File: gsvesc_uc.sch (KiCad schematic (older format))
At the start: 13 parts

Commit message: SCM Fertig
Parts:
- removed C? (x5): 10u0, symbol Device:C
- added C10, C11, C12, C13, C8: 10u0/16V, Capacitor_SMD:C_0805_2012Metric, symbol Device:C
- C3, C4, C5: renamed from C?; footprint (none) -> Capacitor_SMD:C_0805_2012Metric
- C6, C7, C9: renamed from C?; value 10u0 -> 10u0/16V; footprint (none) -> Capacitor_SMD:C_0805_2012Metric
- Y1: renamed from Y?; value Crystal_GND24 -> ABM3B 8MHz; footprint (none) -> Crystal:Crystal_SMD_5032-4Pin_5.0x3.2mm
- gave numbers to parts that had none: 1
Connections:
- net GND: now also C10.1, C11.1, C12.1, C13.1, C8.1
- net VCC: now also C10.2, C11.2, C12.2, C13.2, C8.2
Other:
- moved on the sheet: C6
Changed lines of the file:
@@
 $EndDescr
 $Comp
-L MCU_ST_STM32F4:STM32F405RGTx U?
+L MCU_ST_STM32F4:STM32F405RGTx U1
 U 1 1 5BFF9EEA
 P 4150 4200
-F 0 "U?" H 3600 2450 50  0000 C CNN
+F 0 "U1" H 3600 2450 50  0000 C CNN
 F 1 "STM32F405RGTx" H 3600 2350 50  0000 C CNN
 F 2 "Package_QFP:LQFP-64_10x10mm_P0.5mm" H 3550 2500 50  0001 R CNN
@@
 	3450 5800 3200 5800
 $Comp
-L Device:Crystal_GND24 Y?
+L Device:Crystal_GND24 Y1
 U 1 1 5C00BFEF
 P 1900 3800
-F 0 "Y?" H 1700 4100 50  0000 L CNN
-F 1 "Crystal_GND24" H 1250 4000 50  0000 L CNN
-F 2 "" H 1900 3800 50  0001 C CNN
+F 0 "Y1" H 1700 4100 50  0000 L CNN
+F 1 "ABM3B 8MHz" H 1250 4000 50  0000 L CNN
+F 2 "Crystal:Crystal_SMD_5032-4Pin_5.0x3.2mm" H 1900 3800 50  0001 C CNN
 F 3 "~" H 1900 3800 50  0001 C CNN
 	1    1900 3800
@@
 	2400 3900 3450 3900
 $Comp
-L Device:C C?
+L Device:C C3
 U 1 1 5C0116B6
 P 2250 3600
-F 0 "C?" V 2100 3700 50  0000 C CNN
+F 0 "C3" V 2100 3700 50  0000 C CNN
 F 1 "15p0" V 2200 3750 50  0000 C CNN
-F 2 "" H 2288 3450 50  0001 C CNN
+F 2 "Capacitor_SMD:C_0805_2012Metric" H 2288 3450 50  0001 C CNN
 F 3 "~" H 2250 3600 50  0001 C CNN
 	1    2250 3600
@@
 $EndComp
 $Comp
-L Device:C C?
+L Device:C C4
 U 1 1 5C01170C
 P 2250 4000
-F 0 "C?" V 2200 3850 50  0000 C CNN
+F 0 "C4" V 2200 3850 50  0000 C CNN
 F 1 "15p0" V 2300 3850 50  0000 C CNN
-F 2 "" H 2288 3850 50  0001 C CNN
+F 2 "Capacitor_SMD:C_0805_2012Metric" H 2288 3850 50  0001 C CNN
 F 3 "~" H 2250 4000 50  0001 C CNN
 	1    2250 4000
@@
 	2400 3800 2050 3800
 $Comp
-L Device:C C?
+L Device:C C6
 U 1 1 5C01B300
-P 2750 3300
-F 0 "C?" H 2635 3254 50  0000 R CNN
-F 1 "10u0" H 2635 3345 50  0000 R CNN
-F 2 "" H 2788 3150 50  0001 C CNN
-F 3 "~" H 2750 3300 50  0001 C CNN
-	1    2750 3300
+P 2700 3300
+F 0 "C6" H 2650 3200 50  0000 R CNN
+F 1 "10u0/16V" H 2700 3400 50  0000 R CNN
+F 2 "Capacitor_SMD:C_0805_2012Metric" H 2738 3150 50  0001 C CNN
+F 3 "~" H 2700 3300 50  0001 C CNN
+	1    2700 3300
 	-1   0    0    1
 $EndComp
 $Comp
-L Device:C C?
+L Device:C C7
 U 1 1 5C01B37C
 P 3150 3300
-F 0 "C?" H 3035 3254 50  0000 R CNN
-F 1 "10u0" H 3035 3345 50  0000 R CNN
-F 2 "" H 3188 3150 50  0001 C CNN
+F 0 "C7" H 3150 3200 50  0000 R CNN
+F 1 "10u0/16V" H 3150 3400 50  0000 R CNN
+F 2 "Capacitor_SMD:C_0805_2012Metric" H 3188 3150 50  0001 C CNN
 F 3 "~" H 3150 3300 50  0001 C CNN
 	1    3150 3300
@@
 $EndComp
 Wire Wire Line
-	2750 3000 2750 3150
-Wire Wire Line
-	2750 3450 2750 3550
-Wire Wire Line
-	2750 3550 3150 3550
-Wire Wire Line
 	3150 3550 3150 3450
 $Comp
-L power:GND #PWR?
+L power:GND #PWR022
 U 1 1 5C020C7C
 P 3150 3550
-F 0 "#PWR?" H 3150 3300 50  0001 C CNN
+F 0 "#PWR022" H 3150 3300 50  0001 C CNN
 F 1 "GND" H 3155 3377 50  0000 C CNN
 F 2 "" H 3150 3550 50  0001 C CNN
@@
 Connection ~ 3150 3550
 Wire Wire Line
-	2750 3000 3450 3000
-Wire Wire Line
 	3450 3100 3150 3100
 Wire Wire Line
 	3150 3100 3150 3150
 $Comp
-L power:GND #PWR?
+L power:GND #PWR021
 U 1 1 5C022B75
 P 3150 2800
-F 0 "#PWR?" H 3150 2550 50  0001 C CNN
+F 0 "#PWR021" H 3150 2550 50  0001 C CNN
 F 1 "GND" V 3155 2672 50  0000 R CNN
 F 2 "" H 3150 2800 50  0001 C CNN
@@
 	3150 2800 3450 2800
 $Comp
-L Device:C C?
+L Device:C C5
 U 1 1 5C026BC6
 P 2350 2800
-F 0 "C?" H 2465 2846 50  0000 L CNN
+F 0 "C5" H 2465 2846 50  0000 L CNN
 F 1 "100n" H 2465 2755 50  0000 L CNN
-F 2 "" H 2388 2650 50  0001 C CNN
+F 2 "Capacitor_SMD:C_0805_2012Metric" H 2388 2650 50  0001 C CNN
 F 3 "~" H 2350 2800 50  0001 C CNN
 	1    2350 2800
@@
 	2350 2600 2350 2650
 $Comp
-L power:GND #PWR?
+L power:GND #PWR020
 U 1 1 5C028DBD
 P 2350 2950
-F 0 "#PWR?" H 2350 2700 50  0001 C CNN
+F 0 "#PWR020" H 2350 2700 50  0001 C CNN
 F 1 "GND" H 2355 2777 50  0000 C CNN
 F 2 "" H 2350 2950 50  0001 C CNN
@@
 	5100 4500 4850 4500
 $Comp
-L Device:C C?
-U 1 1 5C030E98
-P 3950 2050
-F 0 "C?" H 3950 2150 50  0000 L CNN
-F 1 "10u0" H 3850 2050 50  0000 L CNN
-F 2 "" H 3988 1900 50  0001 C CNN
-F 3 "~" H 3950 2050 50  0001 C CNN
-	1    3950 2050
-	1    0    0    -1
-$EndComp
-$Comp
-L Device:C C?
+L Device:C C9
 U 1 1 5C030F0E
 P 4050 1750
-F 0 "C?" H 4050 1850 50  0000 L CNN
-F 1 "10u0" H 3950 1750 50  0000 L CNN
-F 2 "" H 4088 1600 50  0001 C CNN
+F 0 "C9" H 4050 1850 50  0000 L CNN
+F 1 "10u0/16V" H 3950 1750 50  0000 L CNN
+F 2 "Capacitor_SMD:C_0805_2012Metric" H 4088 1600 50  0001 C CNN
 F 3 "~" H 4050 1750 50  0001 C CNN
 	1    4050 1750
 	1    0    0    -1
 $EndComp
-$Comp
-L Device:C C?
-U 1 1 5C030F5C
-P 4150 2050
-F 0 "C?" H 4150 2150 50  0000 L CNN
-F 1 "10u0" H 4050 2050 50  0000 L CNN
-F 2 "" H 4188 1900 50  0001 C CNN
-F 3 "~" H 4150 2050 50  0001 C CNN
-	1    4150 2050
-	1    0    0    -1
-$EndComp
-$Comp
-L Device:C C?
-U 1 1 5C031170
-P 4350 2050
-F 0 "C?" H 4350 2150 50  0000 L CNN
-F 1 "10u0" H 4250 2050 50  0000 L CNN
-F 2 "" H 4388 1900 50  0001 C CNN
-F 3 "~" H 4350 2050 50  0001 C CNN
-	1    4350 2050
-	1    0    0    -1
-$EndComp
-$Comp
-L Device:C C?
-U 1 1 5C031202
-P 4250 1750
-F 0 "C?" H 4250 1850 50  0000 L CNN
-F 1 "10u0" H 4150 1750 50  0000 L CNN
-F 2 "" H 4288 1600 50  0001 C CNN
-F 3 "~" H 4250 1750 50  0001 C CNN
-	1    4250 1750
-	1    0    0    -1
-$EndComp
-$Comp
-L Device:C C?
-U 1 1 5C031238
-P 4450 1750
-F 0 "C?" H 4450 1850 50  0000 L CNN
-F 1 "10u0" H 4350 1750 50  0000 L CNN
-F 2 "" H 4488 1600 50  0001 C CNN
-F 3 "~" H 4450 1750 50  0001 C CNN
-	1    4450 1750
-	1    0    0    -1
-$EndComp
 Wire Wire Line
 	3950 2200 3950 2300
@@
 	4350 2400 4350 2300
 $Comp
-L power:VCC #PWR?
+L power:VCC #PWR024
 U 1 1 5C0441EA
 P 3700 2300
-F 0 "#PWR?" H 3700 2150 50  0001 C CNN
+F 0 "#PWR024" H 3700 2150 50  0001 C CNN
 F 1 "VCC" H 3717 2473 50  0000 C CNN
 F 2 "" H 3700 2300 50  0001 C CNN
@@
 Wire Wire Line
 	4050 1600 4150 1600
-Connection ~ 4250 1600
-Wire Wire Line
-	4250 1600 4350 1600
 Wire Wire Line
 	4150 1900 4150 1600
 Connection ~ 4150 1600
 Wire Wire Line
-	4150 1600 4250 1600
-Wire Wire Line
 	4350 1900 4350 1600
 Connection ~ 4350 1600
@@
 Connection ~ 3950 1600
 $Comp
-L power:GND #PWR?
+L power:GND #PWR023
 U 1 1 5C04EECC
 P 3700 1600
-F 0 "#PWR?" H 3700 1350 50  0001 C CNN
+F 0 "#PWR023" H 3700 1350 50  0001 C CNN
 F 1 "GND" H 3705 1427 50  0000 C CNN
 F 2 "" H 3700 1600 50  0001 C CNN
@@
 	4150 6250 4250 6250
 $Comp
-L power:GND #PWR?
+L power:GND #PWR025
 U 1 1 5C068B6D
 P 4150 6250
-F 0 "#PWR?" H 4150 6000 50  0001 C CNN
+F 0 "#PWR025" H 4150 6000 50  0001 C CNN
 F 1 "GND" H 4155 6077 50  0000 C CNN
 F 2 "" H 4150 6250 50  0001 C CNN
@@
 Text Notes 7200 6850 0    157  ~ 0
 Controller
+Wire Wire Line
+	2700 3000 3450 3000
+Wire Wire Line
+	2700 3000 2700 3150
+Wire Wire Line
+	2700 3550 3150 3550
+Wire Wire Line
+	2700 3550 2700 3450
+Wire Wire Line
+	4150 1600 4250 1600
+$Comp
+L Device:C C8
+U 1 1 5C15604C
+P 3950 2050
+F 0 "C8" H 3950 2150 50  0000 L CNN
+F 1 "10u0/16V" H 3850 2050 50  0000 L CNN
+F 2 "Capacitor_SMD:C_0805_2012Metric" H 3988 1900 50  0001 C CNN
+F 3 "~" H 3950 2050 50  0001 C CNN
+	1    3950 2050
+	1    0    0    -1
+$EndComp
+$Comp
+L Device:C C10
+U 1 1 5C156086
+P 4150 2050
+F 0 "C10" H 4150 2150 50  0000 L CNN
+F 1 "10u0/16V" H 4050 2050 50  0000 L CNN
+F 2 "Capacitor_SMD:C_0805_2012Metric" H 4188 1900 50  0001 C CNN
+F 3 "~" H 4150 2050 50  0001 C CNN
+	1    4150 2050
+	1    0    0    -1
+$EndComp
+$Comp
+L Device:C C11
+U 1 1 5C1560BA
+P 4250 1750
+F 0 "C11" H 4250 1850 50  0000 L CNN
+F 1 "10u0/16V" H 4150 1750 50  0000 L CNN
+F 2 "Capacitor_SMD:C_0805_2012Metric" H 4288 1600 50  0001 C CNN
+F 3 "~" H 4250 1750 50  0001 C CNN
+	1    4250 1750
+	1    0    0    -1
+$EndComp
+Connection ~ 4250 1600
+Wire Wire Line
+	4250 1600 4350 1600
+$Comp
+L Device:C C12
+U 1 1 5C1560F2
+P 4350 2050
+F 0 "C12" H 4350 2150 50  0000 L CNN
+F 1 "10u0/16V" H 4250 2050 50  0000 L CNN
+F 2 "Capacitor_SMD:C_0805_2012Metric" H 4388 1900 50  0001 C CNN
+F 3 "~" H 4350 2050 50  0001 C CNN
+	1    4350 2050
+	1    0    0    -1
+$EndComp
+$Comp
+L Device:C C13
+U 1 1 5C156122
+P 4450 1750
+F 0 "C13" H 4450 1850 50  0000 L CNN
+F 1 "10u0/16V" H 4350 1750 50  0000 L CNN
+F 2 "Capacitor_SMD:C_0805_2012Metric" H 4488 1600 50  0001 C CNN
+F 3 "~" H 4450 1750 50  0001 C CNN
+	1    4450 1750
+	1    0    0    -1
+$EndComp
 $EndSCHEMATC

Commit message: Revision 2.0a
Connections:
- net GND: now also C4.1, U1.6 (PH1), Y1.1
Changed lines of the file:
@@
 	1    0    0    -1
 $EndComp
+$Comp
+L power:GND #PWR?
+U 1 1 5C4737D3
+P 2400 4150
+F 0 "#PWR?" H 2400 3900 50  0001 C CNN
+F 1 "GND" H 2405 3977 50  0000 C CNN
+F 2 "" H 2400 4150 50  0001 C CNN
+F 3 "" H 2400 4150 50  0001 C CNN
+	1    2400 4150
+	1    0    0    -1
+$EndComp
+Connection ~ 2400 4150
 $EndSCHEMATC

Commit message: fix some bugs
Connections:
- net USB_D+: now also U1.45 (PA12); no longer U1.44 (PA11)
- net USB_D-: now also U1.44 (PA11); no longer U1.45 (PA12)
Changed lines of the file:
@@
 Text HLabel 5100 3600 2    50   Input ~ 0
 H3
+Text HLabel 5100 3800 2    50   Input ~ 0
+USB_D+
 Text HLabel 5100 3700 2    50   Input ~ 0
-USB_D+
-Text HLabel 5100 3800 2    50   Input ~ 0
 USB_D-
 Text HLabel 5100 3900 2    50   Input ~ 0

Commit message: test
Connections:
- net PB8 is gone; now on net SERVO: U1.61 (PB8)
- net PB9 is gone; now on net FAULT: U1.62 (PB9)
- net FAULT: no longer U1.59 (PB7)
- net SERVO: no longer U1.58 (PB6)
- net NRF_CSN renamed PB12
- net NRF_MISO renamed PD2
- net NRF_MOSI renamed PB3
- net NRF_SCK renamed PB4
- new net P_UART_RX: U1.59 (PB7)
- new net P_UART_TX: U1.58 (PB6)
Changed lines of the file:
@@
 Title "GSVESC - DC Motor Controler"
 Date "2018-11-11"
-Rev "2.0"
+Rev "3.0"
 Comp ""
 Comment1 ""
@@
 Text HLabel 5100 4800 2    50   Input ~ 0
 EN_GATE
-Text HLabel 5100 4900 2    50   Input ~ 0
+Text HLabel 5100 5100 2    50   Input ~ 0
 SERVO
-Text HLabel 5100 5000 2    50   Input ~ 0
+Text HLabel 5100 5200 2    50   Input ~ 0
 FAULT
-Text HLabel 5100 5100 2    50   Input ~ 0
-PB8
-Text HLabel 5100 5200 2    50   Input ~ 0
-PB9
 Text HLabel 5100 5300 2    50   Input ~ 0
 TX_SCL_MOSI
 Text HLabel 5100 5400 2    50   Input ~ 0
 RX_SDA_NSS
-Text HLabel 5100 5500 2    50   Input ~ 0
-NRF_CSN
 Text HLabel 5100 5600 2    50   Input ~ 0
 L1
@@
 Text HLabel 5100 5800 2    50   Input ~ 0
 L3
-Text HLabel 5100 4600 2    50   Input ~ 0
-NRF_MOSI
-Text HLabel 5100 4700 2    50   Input ~ 0
-NRF_SCK
 Text HLabel 3200 4300 0    50   Input ~ 0
 CURRENT_1
@@
 Text HLabel 3200 5500 0    50   Input ~ 0
 SPI3_MOSI
-Text HLabel 3200 4100 0    50   Input ~ 0
-NRF_MISO
 Text HLabel 3200 5600 0    50   Input ~ 0
 HALL_TRIG
@@
 $EndComp
 $Comp
-L power:GND #PWR?
+L power:GND #PWR0101
 U 1 1 5C4737D3
 P 2400 4150
-F 0 "#PWR?" H 2400 3900 50  0001 C CNN
+F 0 "#PWR0101" H 2400 3900 50  0001 C CNN
 F 1 "GND" H 2405 3977 50  0000 C CNN
 F 2 "" H 2400 4150 50  0001 C CNN
@@
 $EndComp
 Connection ~ 2400 4150
+Text HLabel 5100 4600 2    50   Input ~ 0
+PB3
+Text HLabel 5100 4700 2    50   Input ~ 0
+PB4
+Text HLabel 5100 4900 2    50   Input ~ 0
+P_UART_TX
+Text HLabel 5100 5000 2    50   Input ~ 0
+P_UART_RX
+Text HLabel 5100 5500 2    50   Input ~ 0
+PB12
+Text HLabel 3200 4100 0    50   Input ~ 0
+PD2
 $EndSCHEMATC

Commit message: gsesc v3, work in progress
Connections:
- net GND: now also C3.2, Y1.2, Y1.4; no longer U1.6 (PH1), Y1.1
- net at C4.2: now also U1.6 (PH1), Y1.1; no longer Y1.4
- net PD2 renamed CURR_FILTER_ON
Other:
- moved on the sheet: C3, C4
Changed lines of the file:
@@
 $Descr A4 11693 8268
 encoding utf-8
-Sheet 2 6
-Title "GSVESC - DC Motor Controler"
+Sheet 2 5
+Title "GSESC - DC Motor Controler"
 Date "2018-11-11"
 Rev "3.0"
@@
 U 1 1 5C00BFEF
 P 1900 3800
-F 0 "Y1" H 1700 4100 50  0000 L CNN
-F 1 "ABM3B 8MHz" H 1250 4000 50  0000 L CNN
+F 0 "Y1" H 1650 4000 50  0000 L CNN
+F 1 "ABM3B 8MHz" H 1250 3900 50  0000 L CNN
 F 2 "Crystal:Crystal_SMD_5032-4Pin_5.0x3.2mm" H 1900 3800 50  0001 C CNN
 F 3 "~" H 1900 3800 50  0001 C CNN
@@
 $EndComp
 Wire Wire Line
-	3450 3800 2400 3800
-Wire Wire Line
 	1750 3800 1700 3800
 Wire Wire Line
-	1700 3800 1700 4150
-Wire Wire Line
-	1700 4150 2400 4150
-Wire Wire Line
-	2400 4150 2400 4000
-Wire Wire Line
-	2400 3900 3450 3900
+	1700 3800 1700 4050
+Wire Wire Line
+	2700 3900 3450 3900
 $Comp
 L Device:C C3
 U 1 1 5C0116B6
-P 2250 3600
-F 0 "C3" V 2100 3700 50  0000 C CNN
-F 1 "15p0" V 2200 3750 50  0000 C CNN
-F 2 "Capacitor_SMD:C_0805_2012Metric" H 2288 3450 50  0001 C CNN
-F 3 "~" H 2250 3600 50  0001 C CNN
-	1    2250 3600
-	0    1    1    0
+P 2200 3550
+F 0 "C3" V 2050 3650 50  0000 C CNN
+F 1 "15p0" V 2150 3700 50  0000 C CNN
+F 2 "Capacitor_SMD:C_0805_2012Metric" H 2238 3400 50  0001 C CNN
+F 3 "~" H 2200 3550 50  0001 C CNN
+	1    2200 3550
+	-1   0    0    1
 $EndComp
 $Comp
 L Device:C C4
 U 1 1 5C01170C
-P 2250 4000
-F 0 "C4" V 2200 3850 50  0000 C CNN
-F 1 "15p0" V 2300 3850 50  0000 C CNN
-F 2 "Capacitor_SMD:C_0805_2012Metric" H 2288 3850 50  0001 C CNN
-F 3 "~" H 2250 4000 50  0001 C CNN
-	1    2250 4000
-	0    1    1    0
-$EndComp
-Wire Wire Line
-	2100 4000 1900 4000
-Connection ~ 2400 4000
-Wire Wire Line
-	2400 4000 2400 3900
-Wire Wire Line
-	1900 3600 2100 3600
-Wire Wire Line
-	2400 3600 2400 3800
-Connection ~ 2400 3800
-Wire Wire Line
-	2400 3800 2050 3800
+P 1500 3950
+F 0 "C4" V 1450 3800 50  0000 C CNN
+F 1 "15p0" V 1550 3800 50  0000 C CNN
+F 2 "Capacitor_SMD:C_0805_2012Metric" H 1538 3800 50  0001 C CNN
+F 3 "~" H 1500 3950 50  0001 C CNN
+	1    1500 3950
+	-1   0    0    1
+$EndComp
 $Comp
 L Device:C C6
@@
 L power:GND #PWR0101
 U 1 1 5C4737D3
-P 2400 4150
-F 0 "#PWR0101" H 2400 3900 50  0001 C CNN
-F 1 "GND" H 2405 3977 50  0000 C CNN
-F 2 "" H 2400 4150 50  0001 C CNN
-F 3 "" H 2400 4150 50  0001 C CNN
-	1    2400 4150
-	1    0    0    -1
-$EndComp
-Connection ~ 2400 4150
+P 1900 4300
+F 0 "#PWR0101" H 1900 4050 50  0001 C CNN
+F 1 "GND" H 1905 4127 50  0000 C CNN
+F 2 "" H 1900 4300 50  0001 C CNN
+F 3 "" H 1900 4300 50  0001 C CNN
+	1    1900 4300
+	1    0    0    -1
+$EndComp
 Text HLabel 5100 4600 2    50   Input ~ 0
 PB3
@@
 Text HLabel 5100 5500 2    50   Input ~ 0
 PB12
-Text HLabel 3200 4100 0    50   Input ~ 0
-PD2
+Text HLabel 3200 4100 0    50   Output ~ 0
+CURR_FILTER_ON
+Wire Wire Line
+	2050 3800 2200 3800
+Wire Wire Line
+	1700 4050 2700 4050
+Wire Wire Line
+	2700 4050 2700 3900
+Wire Wire Line
+	1700 3800 1500 3800
+Connection ~ 1700 3800
+Wire Wire Line
+	1900 4000 1900 4300
+Wire Wire Line
+	1900 4300 1500 4300
+Wire Wire Line
+	1500 4300 1500 4100
+Connection ~ 1900 4300
+Wire Wire Line
+	2200 3700 2200 3800
+Connection ~ 2200 3800
+Wire Wire Line
+	2200 3800 3450 3800
+Wire Wire Line
+	2200 3400 1900 3400
+Wire Wire Line
+	1900 3400 1900 3600
+$Comp
+L power:GND #PWR0111
+U 1 1 5E360D1D
+P 1900 3400
+F 0 "#PWR0111" H 1900 3150 50  0001 C CNN
+F 1 "GND" H 1905 3227 50  0000 C CNN
+F 2 "" H 1900 3400 50  0001 C CNN
+F 3 "" H 1900 3400 50  0001 C CNN
+	1    1900 3400
+	0    1    1    0
+$EndComp
+Connection ~ 1900 3400
 $EndSCHEMATC

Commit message: V4 first version
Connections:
- net EN_GATE: no longer names the net of U1.57 (PB5)
- net FAULT: no longer names the net of U1.62 (PB9)
- net SPI3_CS renamed SENS_FILTER_ON
- net SPI3_MISO: no longer names the net of U1.52 (PC11)
- net SPI3_MOSI: no longer names the net of U1.53 (PC12)
- net SPI3_SCK: no longer names the net of U1.51 (PC10)
- no-connect marks 0 -> 5
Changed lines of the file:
@@
 $Descr A4 11693 8268
 encoding utf-8
-Sheet 2 5
+Sheet 3 5
 Title "GSESC - DC Motor Controler"
 Date "2018-11-11"
-Rev "3.0"
+Rev "4.0"
 Comp ""
 Comment1 ""
@@
 Text HLabel 5100 4400 2    50   Input ~ 0
 LED_RED
-Text HLabel 5100 4800 2    50   Input ~ 0
-EN_GATE
 Text HLabel 5100 5100 2    50   Input ~ 0
 SERVO
-Text HLabel 5100 5200 2    50   Input ~ 0
-FAULT
 Text HLabel 5100 5300 2    50   Input ~ 0
 TX_SCL_MOSI
@@
 Text HLabel 3200 5100 0    50   Input ~ 0
 HALL_3
-Text HLabel 3200 5200 0    50   Input ~ 0
-SPI3_CS
-Text HLabel 3200 5300 0    50   Input ~ 0
-SPI3_SCK
-Text HLabel 3200 5400 0    50   Input ~ 0
-SPI3_MISO
-Text HLabel 3200 5500 0    50   Input ~ 0
-SPI3_MOSI
 Text HLabel 3200 5600 0    50   Input ~ 0
 HALL_TRIG
@@
 	5100 4700 4850 4700
 Wire Wire Line
-	4850 4800 5100 4800
-Wire Wire Line
 	4850 4900 5100 4900
 Wire Wire Line
@@
 	5100 5100 4850 5100
 Wire Wire Line
-	4850 5200 5100 5200
-Wire Wire Line
 	5100 5300 4850 5300
 Wire Wire Line
@@
 Wire Wire Line
 	3200 5100 3450 5100
-Wire Wire Line
-	3200 5200 3450 5200
-Wire Wire Line
-	3200 5300 3450 5300
-Wire Wire Line
-	3450 5400 3200 5400
-Wire Wire Line
-	3200 5500 3450 5500
 Wire Wire Line
 	3450 5600 3200 5600
@@
 $EndComp
 Connection ~ 1900 3400
+Wire Wire Line
+	3450 5200 3150 5200
+Text HLabel 3150 5200 0    50   Input ~ 0
+SENS_FILTER_ON
+NoConn ~ 4850 4800
+NoConn ~ 4850 5200
+NoConn ~ 3450 5300
+NoConn ~ 3450 5400
+NoConn ~ 3450 5500
 $EndSCHEMATC

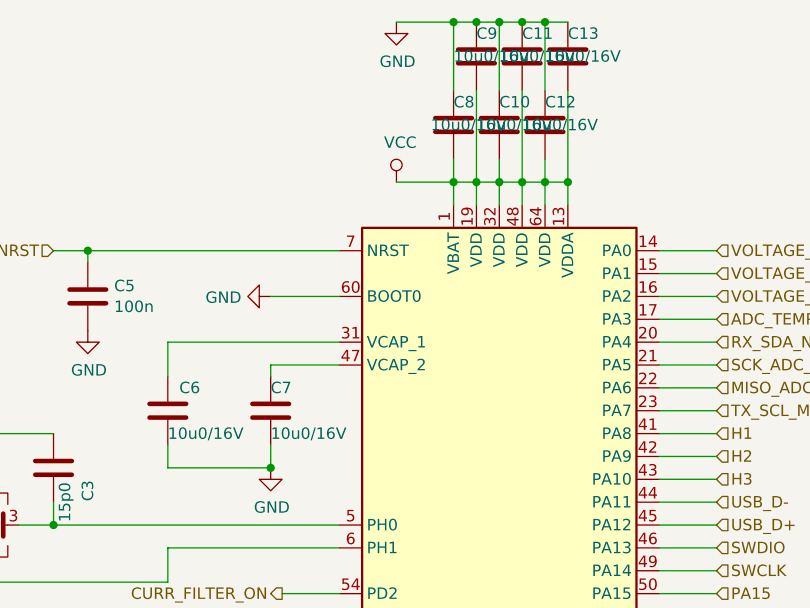
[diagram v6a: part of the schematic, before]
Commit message: Power Supply geändert
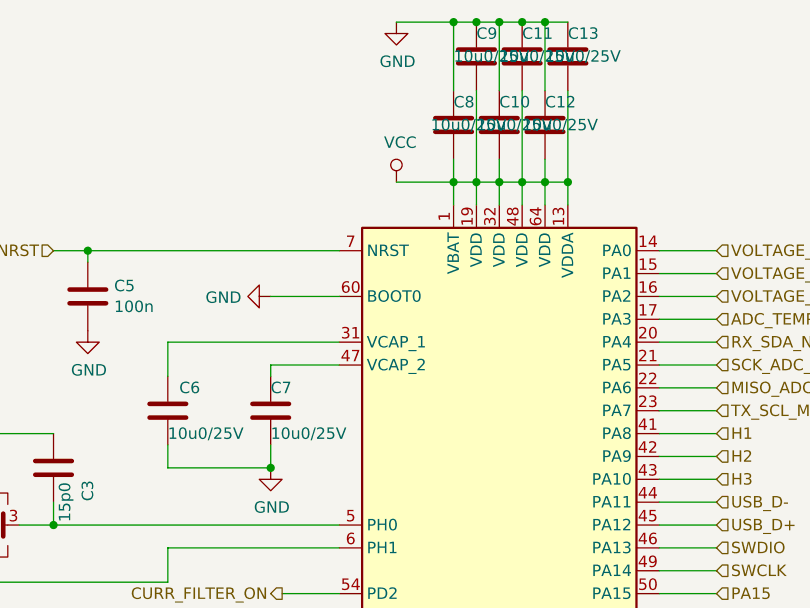
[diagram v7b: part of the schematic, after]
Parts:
- C10, C11, C12, C13, C6, C7, C8, C9: value 10u0/16V -> 10u0/25V
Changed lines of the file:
@@
 P 2700 3300
 F 0 "C6" H 2650 3200 50  0000 R CNN
-F 1 "10u0/16V" H 2700 3400 50  0000 R CNN
+F 1 "10u0/25V" H 2700 3400 50  0000 R CNN
 F 2 "Capacitor_SMD:C_0805_2012Metric" H 2738 3150 50  0001 C CNN
 F 3 "~" H 2700 3300 50  0001 C CNN
@@
 P 3150 3300
 F 0 "C7" H 3150 3200 50  0000 R CNN
-F 1 "10u0/16V" H 3150 3400 50  0000 R CNN
+F 1 "10u0/25V" H 3150 3400 50  0000 R CNN
 F 2 "Capacitor_SMD:C_0805_2012Metric" H 3188 3150 50  0001 C CNN
 F 3 "~" H 3150 3300 50  0001 C CNN
@@
 P 4050 1750
 F 0 "C9" H 4050 1850 50  0000 L CNN
-F 1 "10u0/16V" H 3950 1750 50  0000 L CNN
+F 1 "10u0/25V" H 3950 1750 50  0000 L CNN
 F 2 "Capacitor_SMD:C_0805_2012Metric" H 4088 1600 50  0001 C CNN
 F 3 "~" H 4050 1750 50  0001 C CNN
@@
 P 3950 2050
 F 0 "C8" H 3950 2150 50  0000 L CNN
-F 1 "10u0/16V" H 3850 2050 50  0000 L CNN
+F 1 "10u0/25V" H 3850 2050 50  0000 L CNN
 F 2 "Capacitor_SMD:C_0805_2012Metric" H 3988 1900 50  0001 C CNN
 F 3 "~" H 3950 2050 50  0001 C CNN
@@
 P 4150 2050
 F 0 "C10" H 4150 2150 50  0000 L CNN
-F 1 "10u0/16V" H 4050 2050 50  0000 L CNN
+F 1 "10u0/25V" H 4050 2050 50  0000 L CNN
 F 2 "Capacitor_SMD:C_0805_2012Metric" H 4188 1900 50  0001 C CNN
 F 3 "~" H 4150 2050 50  0001 C CNN
@@
 P 4250 1750
 F 0 "C11" H 4250 1850 50  0000 L CNN
-F 1 "10u0/16V" H 4150 1750 50  0000 L CNN
+F 1 "10u0/25V" H 4150 1750 50  0000 L CNN
 F 2 "Capacitor_SMD:C_0805_2012Metric" H 4288 1600 50  0001 C CNN
 F 3 "~" H 4250 1750 50  0001 C CNN
@@
 P 4350 2050
 F 0 "C12" H 4350 2150 50  0000 L CNN
-F 1 "10u0/16V" H 4250 2050 50  0000 L CNN
+F 1 "10u0/25V" H 4250 2050 50  0000 L CNN
 F 2 "Capacitor_SMD:C_0805_2012Metric" H 4388 1900 50  0001 C CNN
 F 3 "~" H 4350 2050 50  0001 C CNN
@@
 P 4450 1750
 F 0 "C13" H 4450 1850 50  0000 L CNN
-F 1 "10u0/16V" H 4350 1750 50  0000 L CNN
+F 1 "10u0/25V" H 4350 1750 50  0000 L CNN
 F 2 "Capacitor_SMD:C_0805_2012Metric" H 4488 1600 50  0001 C CNN
 F 3 "~" H 4450 1750 50  0001 C CNN
